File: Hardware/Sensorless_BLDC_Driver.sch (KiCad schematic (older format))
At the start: 72 parts, among them J1 POWER, J2 MOTOR, Q1 BUK7M15-60EX, Q2 BUK7M15-60EX, Q3 BUK7M15-60EX, Q4 BUK7M15-60EX, Q5 BUK7M15-60EX, Q6 BUK7M15-60EX, U1 PSoC5LP_Prototyping_Kit, U2 FAN7888

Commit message: [add] add Encoder
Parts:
- added J3: Encoder, KUTKiCad_footprint:Hirose_DF1E_DF1E-5P-2.5DS_1x05_P2.5mm_Vertical, symbol Connector:Conn_01x05_Male
- added RV1, RV2: 10k, Potentiometer_THT:Potentiometer_Alps_RK09K_Single_Vertical, symbol Device:R_POT
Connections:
- net GND: now also J3.2 (Pin_2), RV1.3, RV2.3
- net +5V: now reaches U1.1 (VDD)
- net +5V: now also J3.1 (Pin_1), RV1.1, RV2.1
- net POT_2: now reaches U1.10 (P0_1)
- net POT_2: now also RV2.2
- net POT_1: now reaches U1.11 (P0_0)
- net POT_1: now also RV1.2
- net Index: now reaches U1.38 (P12_4)
- net Index: now also J3.5 (Pin_5)
- net Ch_B: now reaches U1.39 (P12_3)
- net Ch_B: now also J3.4 (Pin_4)
- net Ch_A: now reaches U1.40 (P12_2)
- net Ch_A: now also J3.3 (Pin_3)
- no-connect marks 31 -> 25
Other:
- moved on the sheet: U1

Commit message: PCB chotto susunda
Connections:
- net MOTOR_U: now also J2.1 (Pin_1); no longer J2.3 (Pin_3)
- net MOTOR_W: now also J2.3 (Pin_3); no longer J2.1 (Pin_1)
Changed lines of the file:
@@
 F 4 "DF22-3P-7.92DSA" H 0   0   50  0001 C CNN "MPN"
 	1    10050 3800
-	-1   0    0    1
+	-1   0    0    -1
 $EndComp
 Text GLabel 9750 3900 0    50   Input ~ 0
@@
 $EndComp
 $Comp
-L power:GND #PWR?
+L power:GND #PWR0126
 U 1 1 5EC3107B
 P 7200 3750
-F 0 "#PWR?" H 7200 3500 50  0001 C CNN
+F 0 "#PWR0126" H 7200 3500 50  0001 C CNN
 F 1 "GND" H 7205 3577 50  0000 C CNN
 F 2 "" H 7200 3750 50  0001 C CNN
@@
 $EndComp
 $Comp
-L power:VDD #PWR?
+L power:VDD #PWR0127
 U 1 1 5EC31114
 P 7600 3350
-F 0 "#PWR?" H 7600 3200 50  0001 C CNN
+F 0 "#PWR0127" H 7600 3200 50  0001 C CNN
 F 1 "VDD" H 7617 3523 50  0000 C CNN
 F 2 "" H 7600 3350 50  0001 C CNN
@@
 	6900 3450 7200 3450
 $Comp
-L power:GND #PWR?
+L power:GND #PWR0128
 U 1 1 5EC84488
 P 6900 3750
-F 0 "#PWR?" H 6900 3500 50  0001 C CNN
+F 0 "#PWR0128" H 6900 3500 50  0001 C CNN
 F 1 "GND" H 6905 3577 50  0000 C CNN
 F 2 "" H 6900 3750 50  0001 C CNN
@@
 $EndComp
 $Comp
-L power:+5V #PWR?
+L power:+5V #PWR0129
 U 1 1 5EB05B11
 P 9750 4150
-F 0 "#PWR?" H 9750 4000 50  0001 C CNN
+F 0 "#PWR0129" H 9750 4000 50  0001 C CNN
 F 1 "+5V" H 9765 4323 50  0000 C CNN
 F 2 "" H 9750 4150 50  0001 C CNN
@@
 	9750 4250 9750 4700
 $Comp
-L power:GND #PWR?
+L power:GND #PWR0130
 U 1 1 5EB25E7C
 P 9750 4700
-F 0 "#PWR?" H 9750 4450 50  0001 C CNN
+F 0 "#PWR0130" H 9750 4450 50  0001 C CNN
 F 1 "GND" H 9755 4527 50  0000 C CNN
 F 2 "" H 9750 4700 50  0001 C CNN
@@
 	9400 4550 9850 4550
 $Comp
-L power:+5V #PWR?
+L power:+5V #PWR0131
 U 1 1 5EB698C3
 P 1850 3350
-F 0 "#PWR?" H 1850 3200 50  0001 C CNN
+F 0 "#PWR0131" H 1850 3200 50  0001 C CNN
 F 1 "+5V" H 1865 3523 50  0000 C CNN
 F 2 "" H 1850 3350 50  0001 C CNN
@@
 $EndComp
 $Comp
-L power:+5V #PWR?
+L power:+5V #PWR0132
 U 1 1 5EBF35E8
 P 900 1350
-F 0 "#PWR?" H 900 1200 50  0001 C CNN
+F 0 "#PWR0132" H 900 1200 50  0001 C CNN
 F 1 "+5V" H 915 1523 50  0000 C CNN
 F 2 "" H 900 1350 50  0001 C CNN
@@
 	900  1350 900  1450
 $Comp
-L power:GND #PWR?
+L power:GND #PWR0133
 U 1 1 5EBFEE40
 P 900 1850
-F 0 "#PWR?" H 900 1600 50  0001 C CNN
+F 0 "#PWR0133" H 900 1600 50  0001 C CNN
 F 1 "GND" H 905 1677 50  0000 C CNN
 F 2 "" H 900 1850 50  0001 C CNN
@@
 	900  1850 900  1750
 $Comp
-L power:+5V #PWR?
+L power:+5V #PWR0134
 U 1 1 5EC0A94E
 P 900 2350
-F 0 "#PWR?" H 900 2200 50  0001 C CNN
+F 0 "#PWR0134" H 900 2200 50  0001 C CNN
 F 1 "+5V" H 915 2523 50  0000 C CNN
 F 2 "" H 900 2350 50  0001 C CNN
@@
 	900  2350 900  2450
 $Comp
-L power:GND #PWR?
+L power:GND #PWR0135
 U 1 1 5EC16584
 P 900 2850
-F 0 "#PWR?" H 900 2600 50  0001 C CNN
+F 0 "#PWR0135" H 900 2600 50  0001 C CNN
 F 1 "GND" H 905 2677 50  0000 C CNN
 F 2 "" H 900 2850 50  0001 C CNN

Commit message: [update] delete allover current sense
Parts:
- removed C11: 0.1u, Capacitor_SMD:C_0402_1005Metric, symbol Device:C_Small
- removed R20: 2m, Resistor_SMD:R_0805_2012Metric, symbol Device:R_Small
- removed R21, R22: 4.7, Resistor_SMD:R_0402_1005Metric, symbol Device:R_Small
- renumbered C18 to C11, R32 to R20, R33 to R21, R34 to R22, R35 to R32, R36 to R33
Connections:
- net GND: now also R11.1, R13.1, R14.1, R16.1, R17.1, R19.1
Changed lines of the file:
@@
 	6350 5200 7200 5200
 $Comp
-L Device:R_Small R32
+L Device:R_Small R20
 U 1 1 5EB50576
 P 5600 4600
-F 0 "R32" V 5404 4600 50  0000 C CNN
+F 0 "R20" V 5404 4600 50  0000 C CNN
 F 1 "120" V 5495 4600 50  0000 C CNN
 F 2 "Resistor_SMD:R_0402_1005Metric" H 5600 4600 50  0001 C CNN
@@
 $EndComp
 $Comp
-L Device:R_Small R33
+L Device:R_Small R21
 U 1 1 5EB50898
 P 5600 4900
-F 0 "R33" V 5404 4900 50  0000 C CNN
+F 0 "R21" V 5404 4900 50  0000 C CNN
 F 1 "120" V 5495 4900 50  0000 C CNN
 F 2 "Resistor_SMD:R_0402_1005Metric" H 5600 4900 50  0001 C CNN
@@
 $EndComp
 $Comp
-L Device:R_Small R34
+L Device:R_Small R22
 U 1 1 5EB508FA
 P 5600 5200
-F 0 "R34" V 5404 5200 50  0000 C CNN
+F 0 "R22" V 5404 5200 50  0000 C CNN
 F 1 "120" V 5495 5200 50  0000 C CNN
 F 2 "Resistor_SMD:R_0402_1005Metric" H 5600 5200 50  0001 C CNN
@@
 Wire Wire Line
 	8650 2450 8650 2650
-$Comp
-L Device:R_Small R20
-U 1 1 5EC30B46
-P 5350 2900
-F 0 "R20" H 5291 2854 50  0000 R CNN
-F 1 "2m" H 5291 2945 50  0000 R CNN
-F 2 "Resistor_SMD:R_0805_2012Metric" H 5350 2900 50  0001 C CNN
-F 3 "https://www.rohm.com/datasheet/PMR18EZPFV/pmr-e" H 5350 2900 50  0001 C CNN
-F 4 "Digikey" H 0   0   50  0001 C CNN "Agency"
-F 5 "https://www.digikey.jp/product-detail/ja/rohm-semiconductor/PMR10EZPFV2L00/RHM.002AJCT-ND/2094528" H 0   0   50  0001 C CNN "Link"
-F 6 "PMR10EZPFV2L00" H 0   0   50  0001 C CNN "MPN"
-	1    5350 2900
-	-1   0    0    1
-$EndComp
-$Comp
-L Device:R_Small R21
-U 1 1 5EC30B4E
-P 5100 2750
-F 0 "R21" V 4904 2750 50  0000 C CNN
-F 1 "4.7" V 4995 2750 50  0000 C CNN
-F 2 "Resistor_SMD:R_0402_1005Metric" H 5100 2750 50  0001 C CNN
-F 3 "https://b2b-api.panasonic.eu/file_stream/pids/fileversion/1242" H 5100 2750 50  0001 C CNN
-F 4 "Digkey" H 0   0   50  0001 C CNN "Agency"
-F 5 "https://www.digikey.jp/product-detail/ja/panasonic-electronic-components/ERJ-2GEJ4R7X/P4.7JCT-ND/282380" H 0   0   50  0001 C CNN "Link"
-F 6 "ERJ-2GEJ4R7X" H 0   0   50  0001 C CNN "MPN"
-	1    5100 2750
-	0    1    1    0
-$EndComp
-$Comp
-L Device:C_Small C11
-U 1 1 5EC30B55
-P 4750 2900
-F 0 "C11" H 4658 2854 50  0000 R CNN
-F 1 "0.1u" H 4658 2945 50  0000 R CNN
-F 2 "Capacitor_SMD:C_0402_1005Metric" H 4750 2900 50  0001 C CNN
-F 3 "https://search.murata.co.jp/Ceramy/image/img/A01X/G101/ENG/GRM155R62A104KE14-01.pdf" H 4750 2900 50  0001 C CNN
-F 4 "Digikey" H 0   0   50  0001 C CNN "Agency"
-F 5 "https://www.digikey.jp/product-detail/ja/murata-electronics/GRM155R62A104KE14D/490-10458-1-ND/5026370" H 0   0   50  0001 C CNN "Link"
-F 6 "GRM155R62A104KE14D" H 0   0   50  0001 C CNN "MPN"
-	1    4750 2900
-	-1   0    0    1
-$EndComp
-Wire Wire Line
-	5200 2750 5350 2750
-Connection ~ 5350 2750
-Wire Wire Line
-	5350 2750 5350 2800
-Wire Wire Line
-	4750 3050 4750 3000
-Wire Wire Line
-	4750 2800 4750 2750
-Wire Wire Line
-	4750 2750 5000 2750
-Connection ~ 4750 2750
-Text Label 4450 2750 0    50   ~ 0
-ISH
-Wire Wire Line
-	4450 2750 4750 2750
-Wire Wire Line
-	5350 3000 5350 3050
-$Comp
-L Device:R_Small R22
-U 1 1 5EC30B66
-P 5100 3050
-F 0 "R22" V 4904 3050 50  0000 C CNN
-F 1 "4.7" V 4995 3050 50  0000 C CNN
-F 2 "Resistor_SMD:R_0402_1005Metric" H 5100 3050 50  0001 C CNN
-F 3 "https://b2b-api.panasonic.eu/file_stream/pids/fileversion/1242" H 5100 3050 50  0001 C CNN
-F 4 "Digkey" H 0   0   50  0001 C CNN "Agency"
-F 5 "https://www.digikey.jp/product-detail/ja/panasonic-electronic-components/ERJ-2GEJ4R7X/P4.7JCT-ND/282380" H 0   0   50  0001 C CNN "Link"
-F 6 "ERJ-2GEJ4R7X" H 0   0   50  0001 C CNN "MPN"
-	1    5100 3050
-	0    1    1    0
-$EndComp
-Wire Wire Line
-	5000 3050 4750 3050
-Wire Wire Line
-	5200 3050 5350 3050
-Wire Wire Line
-	4750 3050 4450 3050
-Connection ~ 4750 3050
-Text Label 4450 3050 0    50   ~ 0
-ISL
 Wire Wire Line
 	7000 2650 5350 2650
@@
 Connection ~ 7000 2650
 Connection ~ 5350 2450
-Wire Wire Line
-	5350 2650 5350 2750
-Connection ~ 5350 2650
-Wire Wire Line
-	5350 3050 5350 3200
-Connection ~ 5350 3050
-$Comp
-L power:GND #PWR0108
-U 1 1 5EC720E0
-P 5350 3200
-F 0 "#PWR0108" H 5350 2950 50  0001 C CNN
-F 1 "GND" H 5355 3027 50  0000 C CNN
-F 2 "" H 5350 3200 50  0001 C CNN
-F 3 "" H 5350 3200 50  0001 C CNN
-	1    5350 3200
-	1    0    0    -1
-$EndComp
 $Comp
 L Connector:TestPoint_Probe TP1
@@
 $EndComp
 $Comp
-L Device:R_Small R35
+L Device:R_Small R32
 U 1 1 5EC26916
 P 7400 3450
-F 0 "R35" V 7204 3450 50  0000 C CNN
+F 0 "R32" V 7204 3450 50  0000 C CNN
 F 1 "33k" V 7295 3450 50  0000 C CNN
 F 2 "Resistor_SMD:R_0402_1005Metric" H 7400 3450 50  0001 C CNN
@@
 $EndComp
 $Comp
-L Device:R_Small R36
+L Device:R_Small R33
 U 1 1 5EC26C1E
 P 7200 3650
-F 0 "R36" H 7141 3604 50  0000 R CNN
+F 0 "R33" H 7141 3604 50  0000 R CNN
 F 1 "10k" H 7141 3695 50  0000 R CNN
 F 2 "Resistor_SMD:R_0402_1005Metric" H 7200 3650 50  0001 C CNN
@@
 VS
 $Comp
-L Device:C_Small C18
+L Device:C_Small C11
 U 1 1 5EC64C4E
 P 6900 3650
-F 0 "C18" H 6808 3604 50  0000 R CNN
+F 0 "C11" H 6808 3604 50  0000 R CNN
 F 1 "0.1u" H 6808 3695 50  0000 R CNN
 F 2 "Capacitor_SMD:C_0402_1005Metric" H 6900 3650 50  0001 C CNN
@@
 Text Label 2050 2650 2    50   ~ 0
 POT_2
+$Comp
+L power:GND #PWR?
+U 1 1 5EB6F4C6
+P 5350 2650
+F 0 "#PWR?" H 5350 2400 50  0001 C CNN
+F 1 "GND" H 5355 2477 50  0000 C CNN
+F 2 "" H 5350 2650 50  0001 C CNN
+F 3 "" H 5350 2650 50  0001 C CNN
+	1    5350 2650
+	1    0    0    -1
+$EndComp
+Connection ~ 5350 2650
 $EndSCHEMATC

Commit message: [update] PCB pattern complete
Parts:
- removed TP1: BEMF1, TestPoint:TestPoint_THTPad_D1.0mm_Drill0.5mm, symbol Connector:TestPoint_Probe
- removed TP2: BEMF2, TestPoint:TestPoint_THTPad_D1.0mm_Drill0.5mm, symbol Connector:TestPoint_Probe
- removed TP3: BEMF3, TestPoint:TestPoint_THTPad_D1.0mm_Drill0.5mm, symbol Connector:TestPoint_Probe
- removed TP4: BEMFN, TestPoint:TestPoint_THTPad_D1.0mm_Drill0.5mm, symbol Connector:TestPoint_Probe
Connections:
- net ISH is gone; now on net BEMF1: U1.19 (P3_6)
- net BEMF1: now also R29.2; no longer U1.34 (P2_7)
- net BEMF2: now also R30.2, U1.20 (P3_5); no longer U1.33 (P2_6)
- net BEMF3: now also R31.2, U1.21 (P3_4); no longer U1.32 (P2_5)
- net BEMF_N: now also U1.22 (P3_3); no longer U1.31 (P2_4)
- net Ch_A: now also U1.49 (P1_6); no longer U1.40 (P12_2)
- net Ch_B: now also U1.48 (P1_5); no longer U1.39 (P12_3)
- net HIN_1: now also U1.27 (P2_0); no longer U1.43 (P1_0)
- net HIN_2: now also U1.29 (P2_2); no longer U1.45 (P1_2)
- net HIN_3: now also U1.31 (P2_4); no longer U1.47 (P1_4)
- net ISH_1: now also U1.15 (P15_2); no longer U1.17 (P15_0)
- net ISH_2: now also U1.12 (P15_5); no longer U1.15 (P15_2)
- net ISH_3: now also U1.10 (P0_1); no longer U1.13 (P15_4)
- net ISL_1: now also U1.14 (P15_3); no longer U1.16 (P15_1)
- net ISL_2: now also U1.13 (P15_4); no longer U1.14 (P15_3)
- net ISL_3: now also U1.11 (P0_0); no longer U1.12 (P15_5)
- net Index: now also U1.47 (P1_4); no longer U1.38 (P12_4)
- net LIN_1: now also U1.28 (P2_1); no longer U1.44 (P1_1)
- net LIN_2: now also U1.30 (P2_3); no longer U1.46 (P1_3)
- net LIN_3: now also U1.32 (P2_5); no longer U1.48 (P1_5)
- net POT_1: now also U1.34 (P2_7); no longer U1.11 (P0_0)
- net POT_2: now also U1.45 (P1_2); no longer U1.10 (P0_1)
- net VS: now also U1.24 (P3_1)
- net at R20.1, R23.2, R26.2: no longer R29.2
- net at R21.1, R24.2, R27.2: no longer R30.2
- net at R22.1, R25.2, R28.2: no longer R31.2
- net ISL: no longer names the net of U1.18 (P3_7)
- no-connect marks 25 -> 20
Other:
- moved on the sheet: R20, R21, R22, U1

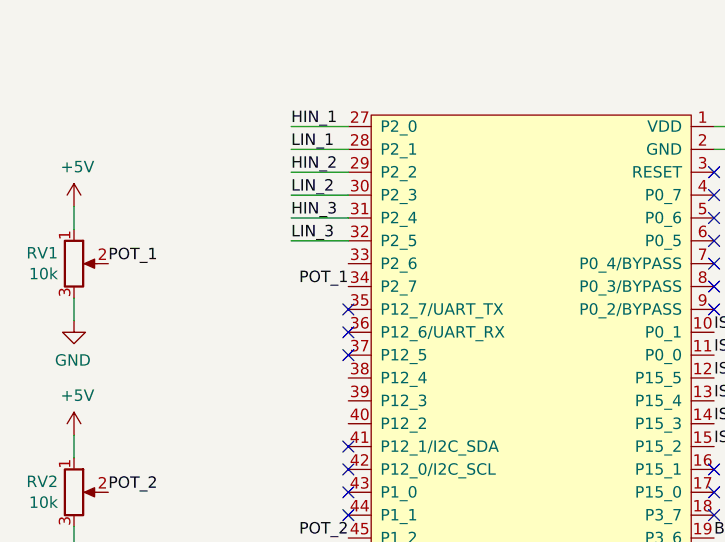
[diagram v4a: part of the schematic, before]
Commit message: [update] adjust silk
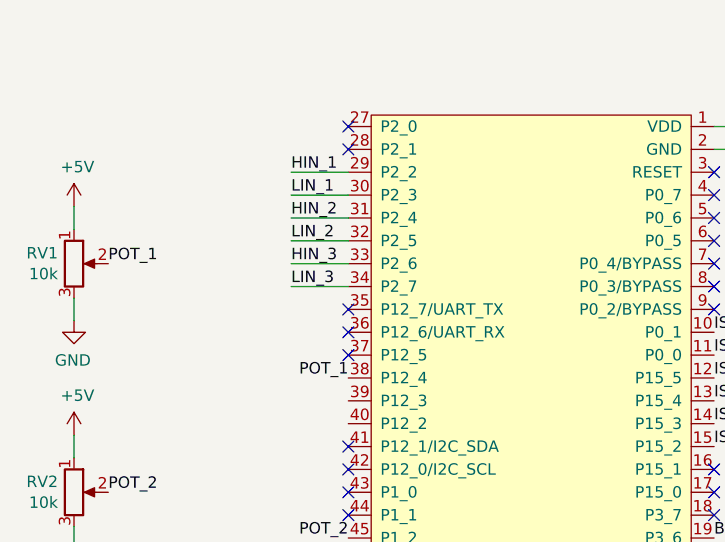
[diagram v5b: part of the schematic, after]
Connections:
- net HIN_1: now also U1.29 (P2_2); no longer U1.27 (P2_0)
- net HIN_2: now also U1.31 (P2_4); no longer U1.29 (P2_2)
- net HIN_3: now also U1.33 (P2_6); no longer U1.31 (P2_4)
- net LIN_1: now also U1.30 (P2_3); no longer U1.28 (P2_1)
- net LIN_2: now also U1.32 (P2_5); no longer U1.30 (P2_3)
- net LIN_3: now also U1.34 (P2_7); no longer U1.32 (P2_5)
- net POT_1: now also U1.38 (P12_4); no longer U1.34 (P2_7)
- no-connect marks 20 -> 22
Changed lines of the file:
@@
 Wire Wire Line
 	9750 3100 9850 3100
-Text Label 1850 1000 0    50   ~ 0
+Text Label 1850 1200 0    50   ~ 0
 HIN_1
-Text Label 1850 1100 0    50   ~ 0
+Text Label 1850 1300 0    50   ~ 0
 LIN_1
-Text Label 1850 1200 0    50   ~ 0
+Text Label 1850 1400 0    50   ~ 0
 HIN_2
-Text Label 1850 1300 0    50   ~ 0
+Text Label 1850 1500 0    50   ~ 0
 LIN_2
-Text Label 1850 1400 0    50   ~ 0
+Text Label 1850 1600 0    50   ~ 0
 HIN_3
-Text Label 1850 1500 0    50   ~ 0
+Text Label 1850 1700 0    50   ~ 0
 LIN_3
 Wire Wire Line
-	2100 1000 1850 1000
-Wire Wire Line
-	1850 1100 2100 1100
-Wire Wire Line
 	2100 1200 1850 1200
 Wire Wire Line
 	1850 1300 2100 1300
 Wire Wire Line
-	1850 1400 2100 1400
+	2100 1400 1850 1400
 Wire Wire Line
 	1850 1500 2100 1500
+Wire Wire Line
+	1850 1600 2100 1600
+Wire Wire Line
+	1850 1700 2100 1700
 Text Label 3700 2800 0    50   ~ 0
 BEMF1
@@
 Text Label 1050 2600 0    50   ~ 0
 POT_2
-Text Label 2100 1700 2    50   ~ 0
+Text Label 2100 2100 2    50   ~ 0
 POT_1
 Text Label 2100 2800 2    50   ~ 0
@@
 NoConn ~ 3700 2600
 NoConn ~ 3700 2700
+NoConn ~ 2100 1000
+NoConn ~ 2100 1100
 $EndSCHEMATC
